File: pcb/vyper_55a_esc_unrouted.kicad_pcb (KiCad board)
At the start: 6 copper layers, 43 x 43 mm, 199 parts, among them J1 FC_ESC_SH1.0_8P, J2 M1_SWD_PADS, J3 M2_SWD_PADS, J4 M3_SWD_PADS, J5 M4_SWD_PADS, Q11 BSC012N06NS, Q12 BSC012N06NS, Q13 BSC012N06NS, Q14 BSC012N06NS, Q15 BSC012N06NS, Q16 BSC012N06NS, Q21 BSC012N06NS, Q22 BSC012N06NS, Q23 BSC012N06NS, Q24 BSC012N06NS, Q25 BSC012N06NS, Q26 BSC012N06NS, Q31 BSC012N06NS, Q32 BSC012N06NS, Q33 BSC012N06NS, Q34 BSC012N06NS, Q35 BSC012N06NS, Q36 BSC012N06NS, Q41 BSC012N06NS, Q42 BSC012N06NS, Q43 BSC012N06NS, Q44 BSC012N06NS, Q45 BSC012N06NS, Q46 BSC012N06NS, U1 LMR16006XDDCR, U11 AT32F421K8U7-4, U12 DRV8323HRTAR, U2 TLV9061IDBVR, U21 AT32F421K8U7-4, U22 DRV8323HRTAR, U31 AT32F421K8U7-4, U32 DRV8323HRTAR, U41 AT32F421K8U7-4, U42 DRV8323HRTAR

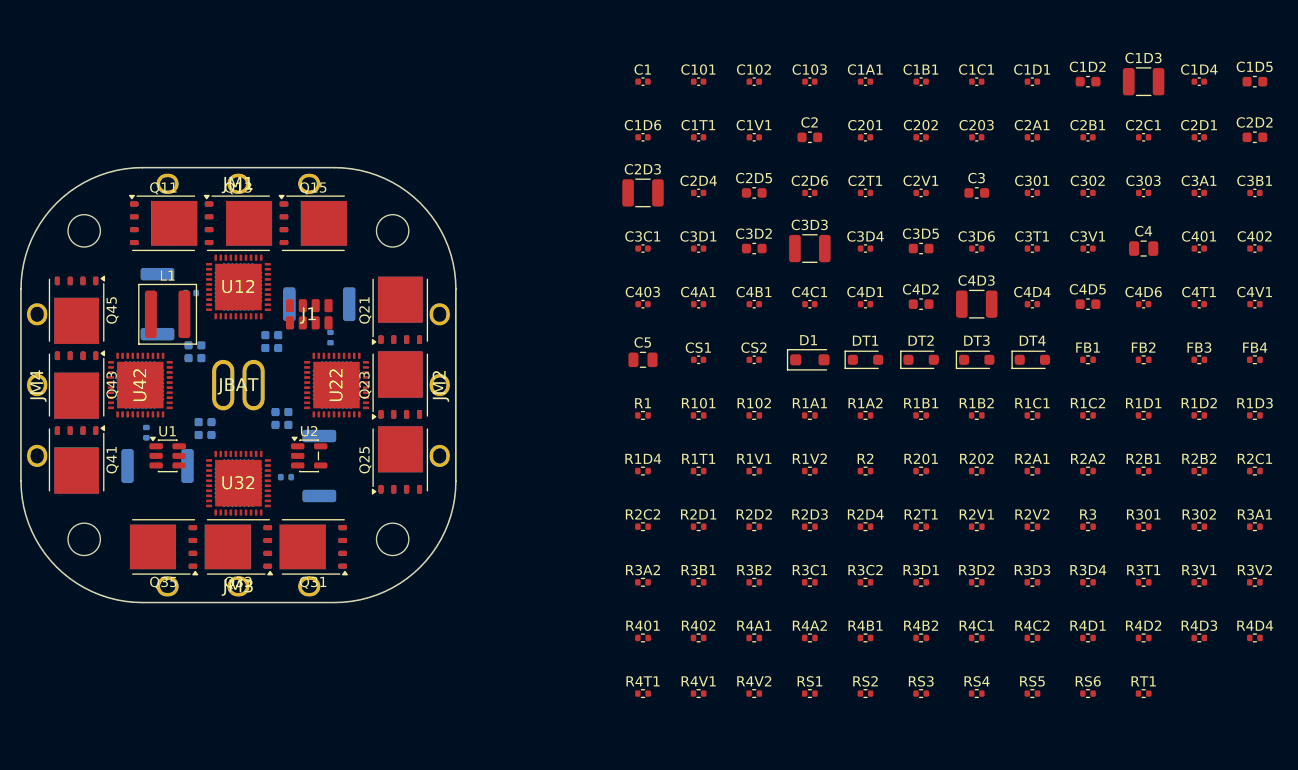
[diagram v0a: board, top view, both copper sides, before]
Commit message: Redesign VYPER around vertical dense electronics
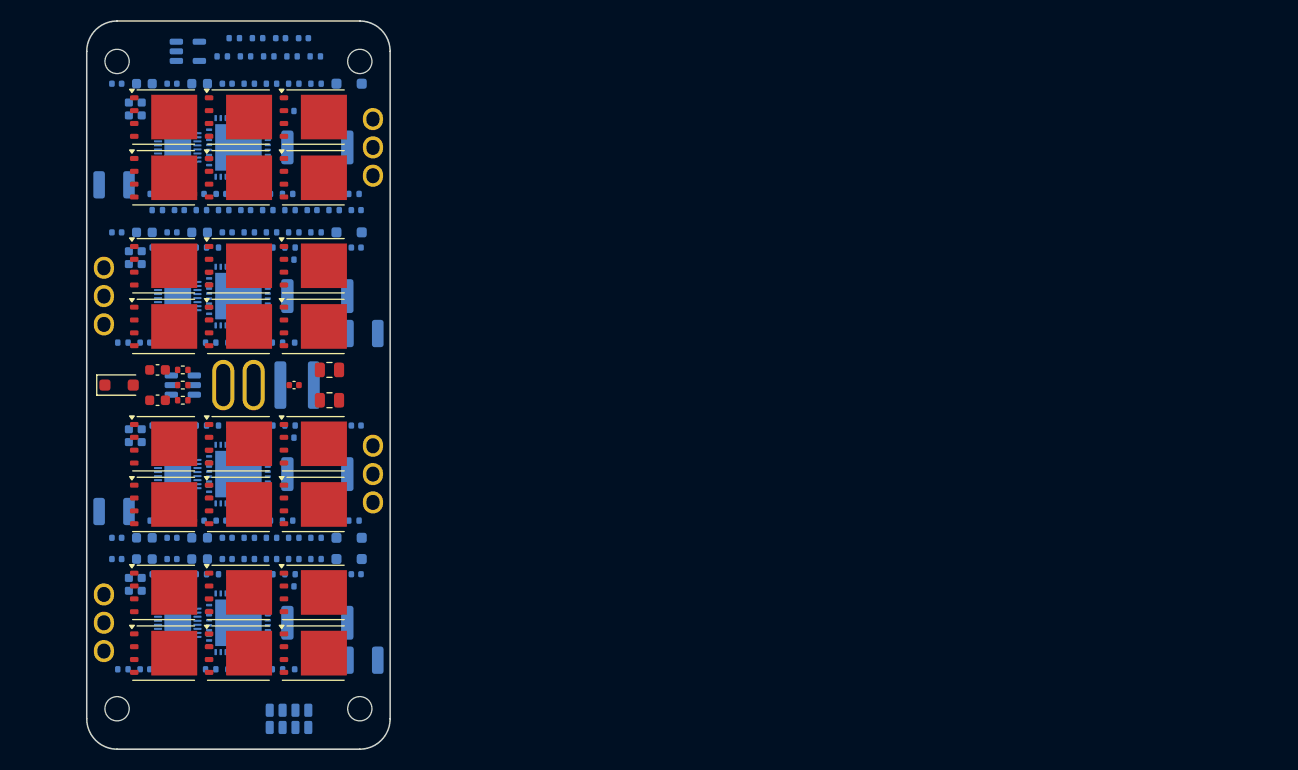
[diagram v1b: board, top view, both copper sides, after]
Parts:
- C101, C102, C103, C1A1, C1B1, C1C1, C1D1, C1D2, C1D3, C1D4, C1D5, C1D6, C1T1, C1V1, C201, C202, C203, C2A1, C2B1, C2C1, C2D1, C2D2, C2D3, C2D4, C2D5, C2D6, C2T1, C2V1, C301, C302, C303, C3A1, C3B1, C3C1, C3D1, C3D2, C3D3, C3D4, C3D5, C3D6, C3T1, C3V1, C401, C402, C403, C4A1, C4B1, C4C1, C4D1, C4D2, C4D3, C4D4, C4D5, C4D6, C4T1, C4V1, CS1, CS2, DT1, DT2, DT3, DT4, FB1, FB2, FB3, FB4, J1, L1, R101, R102, R1A1, R1A2, R1B1, R1B2, R1C1, R1C2, R1D1, R1D2, R1D3, R1D4, R1T1, R1V1, R1V2, R201, R202, R2A1, R2A2, R2B1, R2B2, R2C1, R2C2, R2D1, R2D2, R2D3, R2D4, R2T1, R2V1, R2V2, R301, R302, R3A1, R3A2, R3B1, R3B2, R3C1, R3C2, R3D1, R3D2, R3D3, R3D4, R3T1, R3V1, R3V2, R401, R402, R4A1, R4A2, R4B1, R4B2, R4C1, R4C2, R4D1, R4D2, R4D3, R4D4, R4T1, R4V1, R4V2, RS1, RS2, RS3, RS4, RS5, RS6, RT1, U1, U12, U2, U22, U32, U42: moved to B.Cu
- Q12, Q14, Q16, Q22, Q24, Q26, Q32, Q34, Q36, Q42, Q44, Q46: moved to F.Cu
- moved C2D2 116.7 mm to (-9.30, 15.1)
- moved C1D5 114.5 mm to (-3.84, 17.2)
- moved C2D1 114.1 mm to (-12.0, 15.1)
- moved C1D4 112.0 mm to (-6.57, 17.2)
- moved RT1 110.8 mm to (-1.60, -32.5)
- moved FB4 109.9 mm to (-8.22, -18.9)
- moved R4D4 107.8 mm to (7.67, -29.8)
- moved C3B1 106.5 mm to (-5.84, -13.6)
- moved FB3 106.4 mm to (-11.4, -4.20)
- moved R4D3 105.0 mm to (5.47, -29.8)
- moved RS6 104.6 mm to (1.89, -34.3)
- moved C1D2 104.6 mm to (-9.30, 17.2)
- moved C402 104.5 mm to (-3.88, -18.9)
- moved R2C1 104.3 mm to (-3.66, 4.00)
- moved R2B2 103.1 mm to (-8.02, 4.00)
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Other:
- board size 43 x 43 mm -> 30 x 72 mm
- board text removed: "VYPER-55A EVT / NOT FOR FAB"

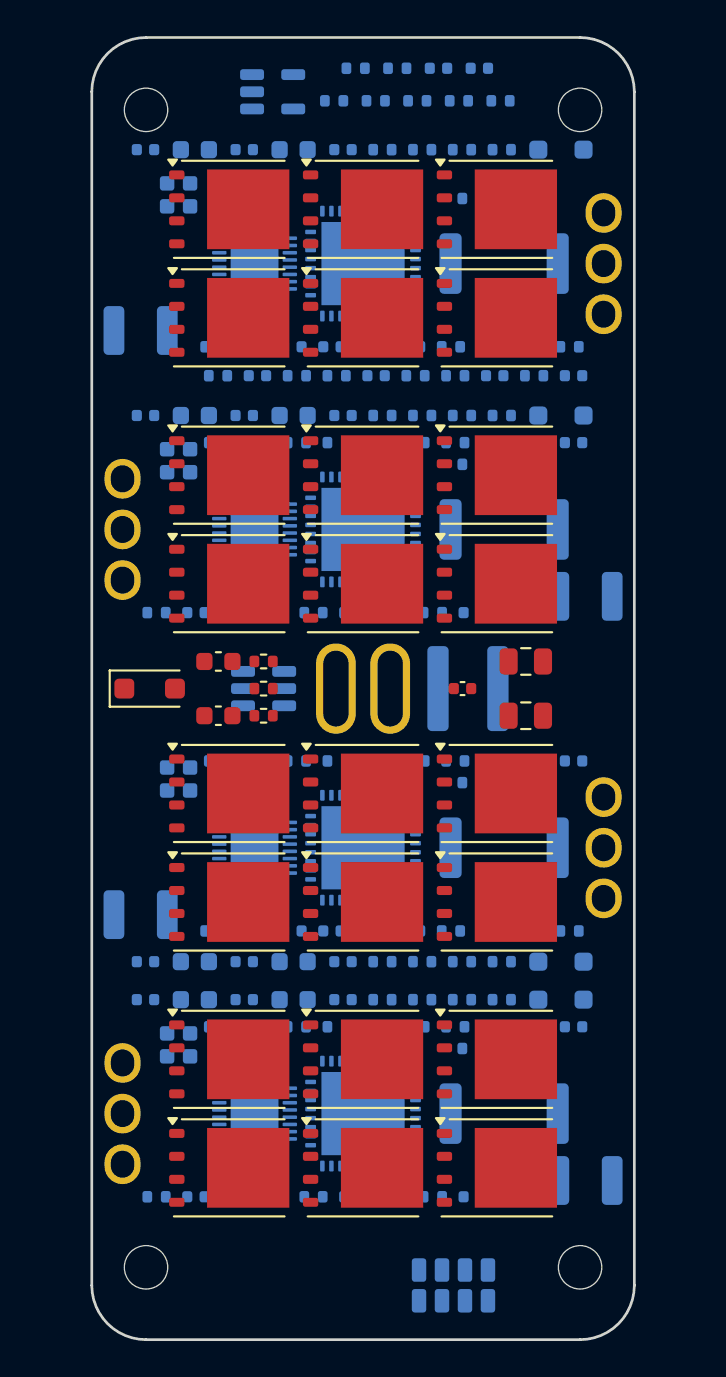
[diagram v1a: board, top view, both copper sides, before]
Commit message: Add production-size wire pads and reproducible PETG slicing
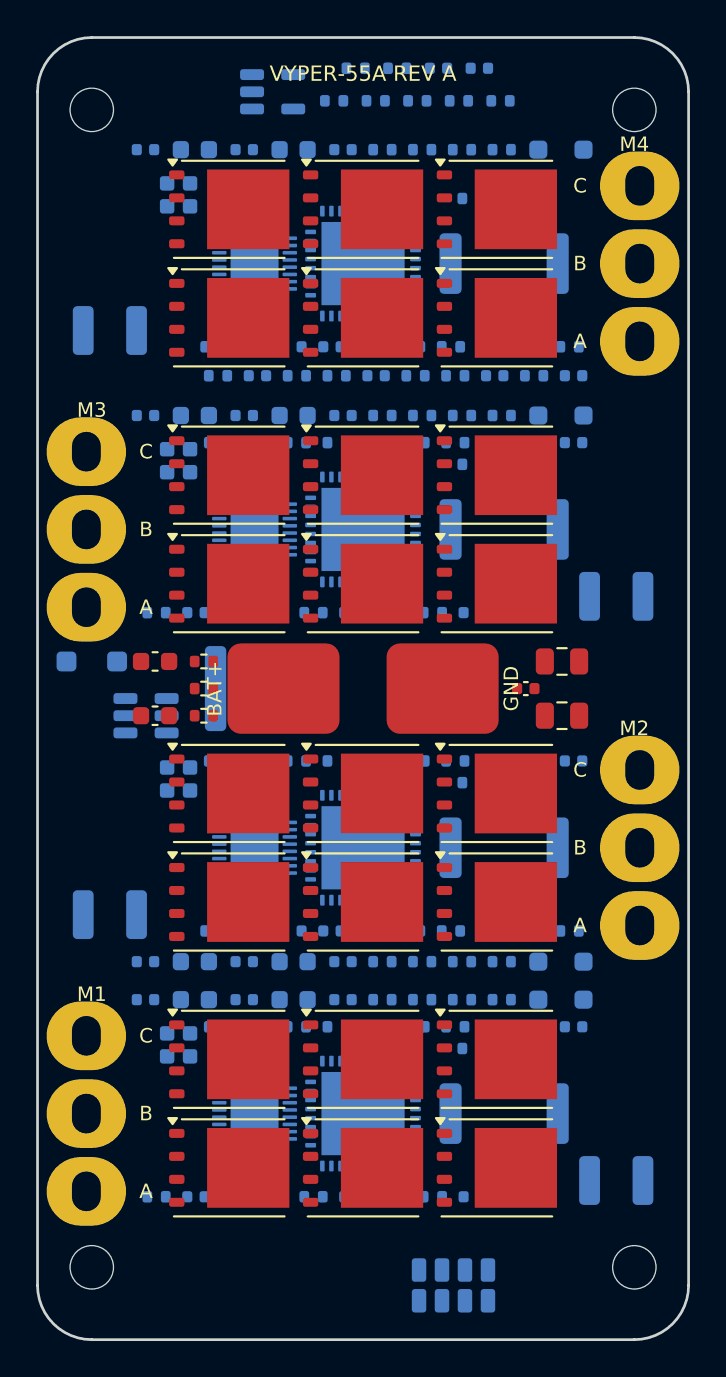
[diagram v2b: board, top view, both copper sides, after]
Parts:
- D1: moved to B.Cu
- moved L1 12.3 mm to (-6.50, 0.00)
- moved U1 6.67 mm to (-12.0, 1.50)
- moved D1 3.53 mm to (-15.0, -1.50)
- moved C1 3.50 mm to (9.00, 0.00)
- moved C2 3.50 mm to (-11.5, 1.50)
- moved C3 3.50 mm to (-11.5, -1.50)
- moved R1 3.30 mm to (-8.80, 1.50)
- moved R2 3.30 mm to (-8.80, 0.00)
- moved R3 3.30 mm to (-8.80, -1.50)
- moved H1 3.00 mm to (-15.0, 32.0)
- moved H2 3.00 mm to (-15.0, -32.0)
- moved H3 3.00 mm to (15.0, 32.0)
- moved H4 3.00 mm to (15.0, -32.0)
- moved C4 2.00 mm to (11.0, 1.50)
- moved C5 2.00 mm to (11.0, -1.50)
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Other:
- board size 30 x 72 mm -> 36 x 72 mm
- board text added: "A"
- board text added: "B"
- board text added: "BAT+"
- board text added: "C"
- board text added: "GND"
- board text added: "M1"
- board text added: "M2"
- board text added: "M3"
- board text added: "M4"
- board text added: "VYPER-55A REV A"
